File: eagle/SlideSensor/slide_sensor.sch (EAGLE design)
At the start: 12 parts

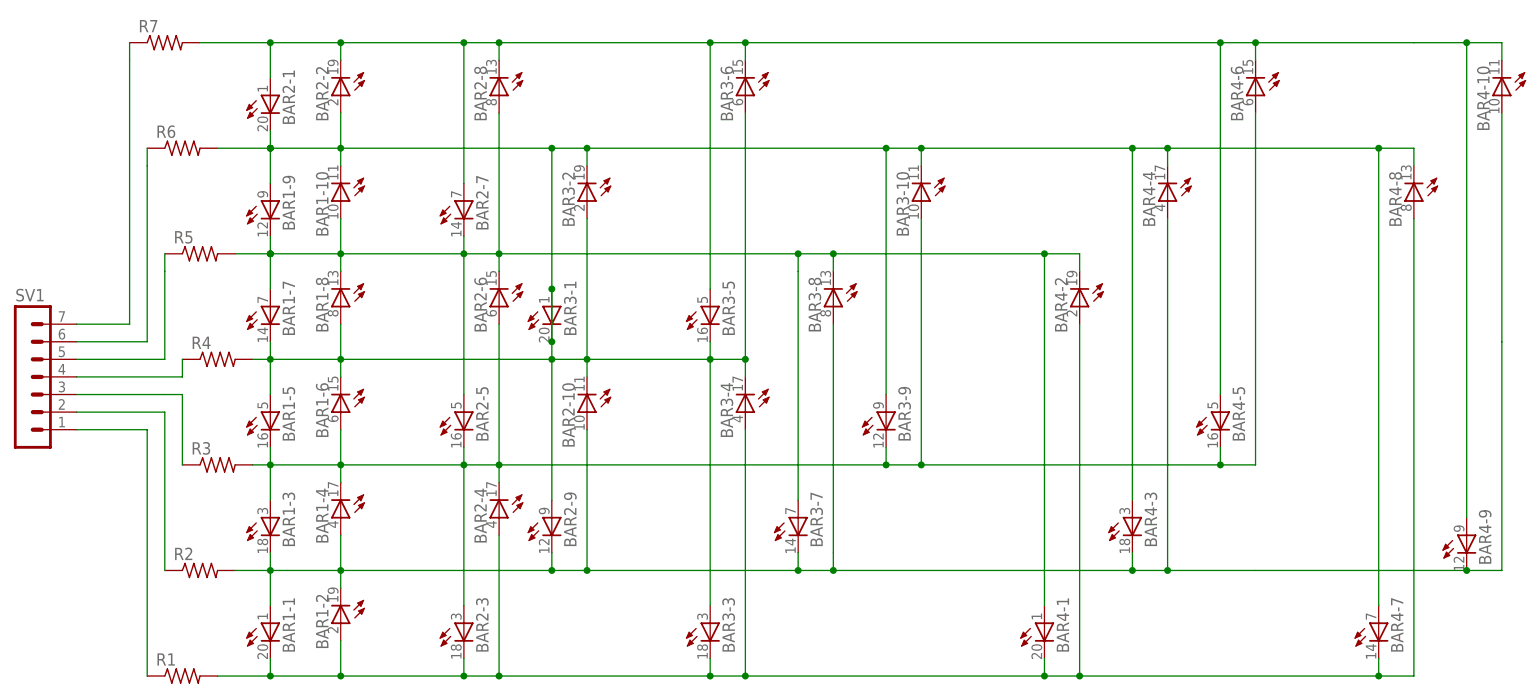
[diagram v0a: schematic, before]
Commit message: v2 - fix bad schematic
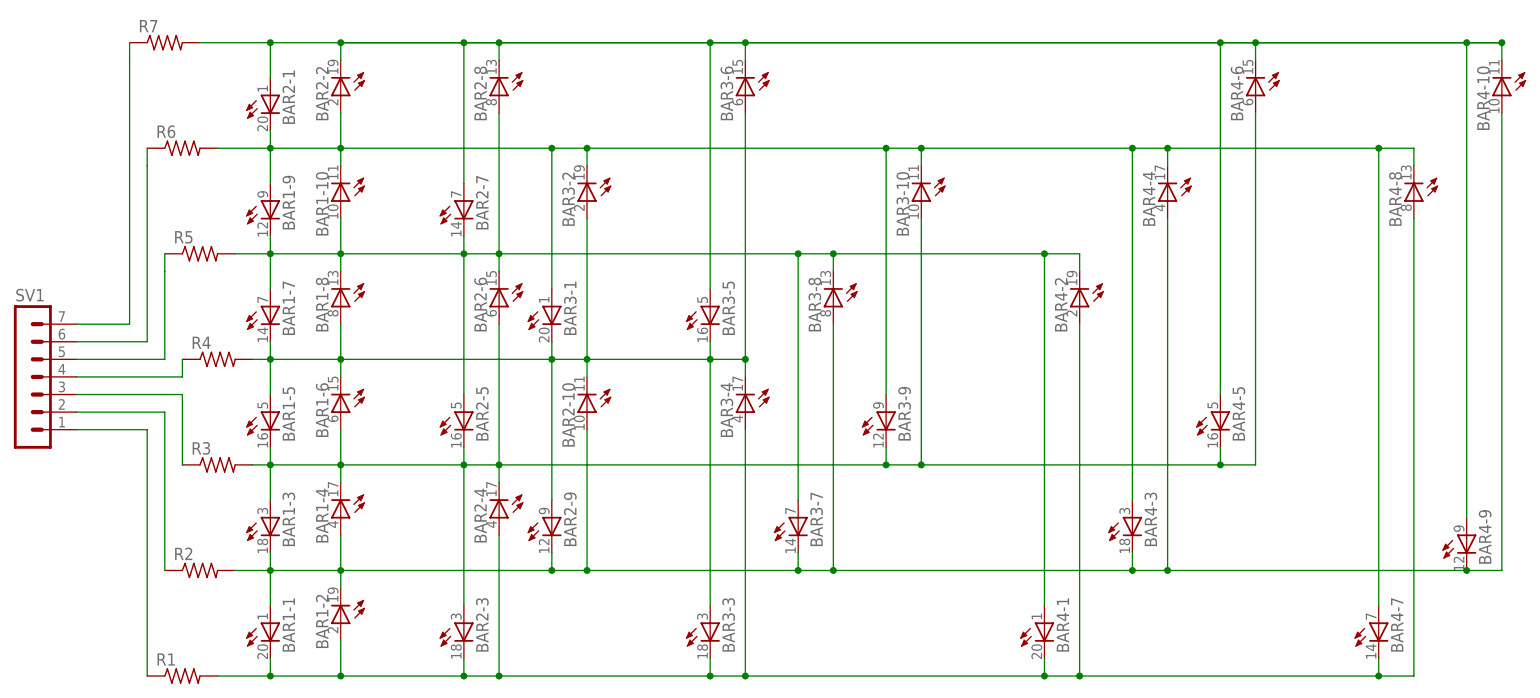
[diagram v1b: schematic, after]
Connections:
- net N$11 renamed N$L7
- net N$17 renamed N$P6
- net N$21 renamed N$P5
- net N$23 renamed N$L5
- net N$25 renamed N$P3
- net N$3 renamed N$P4
- net N$4 renamed N$P2
- net N$5 renamed N$L2
- net N$6 renamed N$L1
- net N$7 renamed N$P7
- net N$8 renamed N$P1
- removed net N$9: BAR1-10.C, BAR1-3.A, BAR1-4.C, BAR1-5.A, BAR1-5.C, BAR1-6.A, BAR1-6.C, BAR1-7.C, BAR1-8.A, BAR1-9.A, BAR2-1.C, BAR2-10.C, BAR2-2.A, BAR2-3.A, BAR2-4.C, BAR2-5.C, BAR2-6.A, BAR2-9.A, BAR3-1.A, BAR3-1.C, BAR3-10.A, BAR3-10.C, BAR3-2.A, BAR3-2.C, BAR3-3.A, BAR3-4.C, BAR3-5.C, BAR3-6.A, BAR3-9.A, BAR3-9.C, BAR4-3.A, BAR4-4.C, BAR4-5.C, BAR4-6.A, BAR4-7.A, BAR4-8.C, R3.2, R4.2, R6.2
- new net N$L3: BAR1-3.A, BAR1-4.C, BAR1-5.C, BAR1-6.A, BAR2-3.A, BAR2-4.C, BAR2-5.C, BAR2-6.A, BAR3-10.A, BAR3-9.C, BAR4-5.C, BAR4-6.A, R3.2
- new net N$L4: BAR1-5.A, BAR1-6.C, BAR1-7.C, BAR1-8.A, BAR2-10.C, BAR2-9.A, BAR3-1.C, BAR3-2.A, BAR3-3.A, BAR3-4.C, BAR3-5.C, BAR3-6.A, R4.2
- new net N$L6: BAR1-10.C, BAR1-9.A, BAR2-1.C, BAR2-2.A, BAR3-1.A, BAR3-10.C, BAR3-2.C, BAR3-9.A, BAR4-3.A, BAR4-4.C, BAR4-7.A, BAR4-8.C, R6.2
